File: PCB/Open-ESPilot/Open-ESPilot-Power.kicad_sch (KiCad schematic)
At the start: 29 parts, among them J15 VOUT, J2 VIN, J3 GND, M1 Clone "MP1584" module, Q3 AO3401A, U2 AMS1117-3.3, U3 INA219AxD, U8 AMS1117-3.3

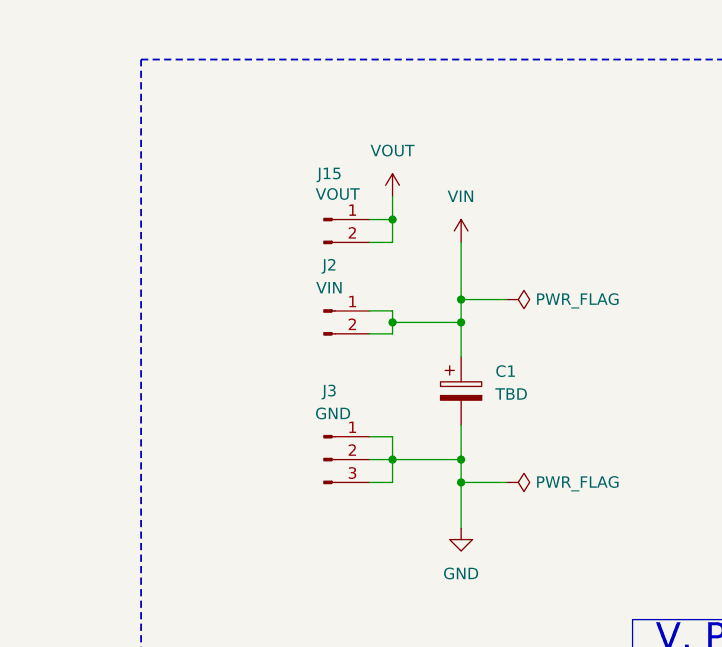
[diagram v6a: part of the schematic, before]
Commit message: Assigned footprints and components for the easy ones (R,C,JP,J)
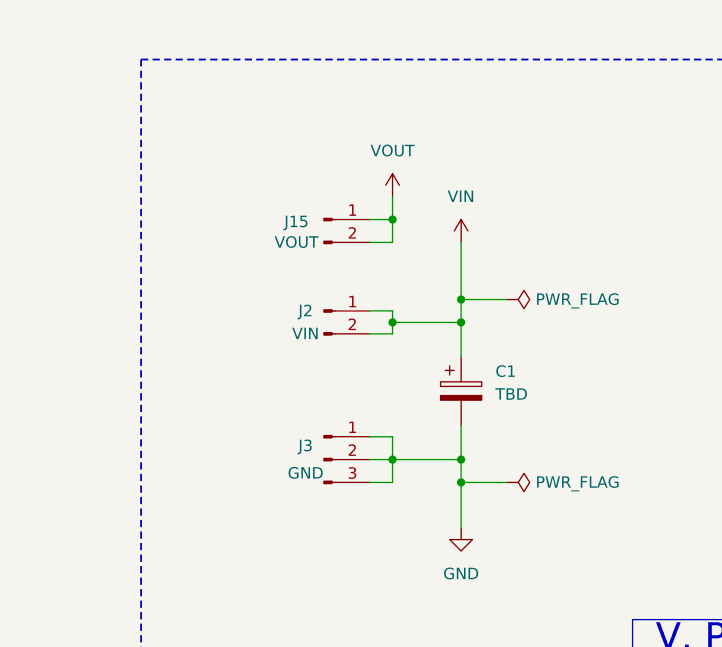
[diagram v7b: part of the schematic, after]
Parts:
- C10, C11, C12, C6, C7: footprint (none) -> Capacitor_SMD:C_0805_2012Metric_Pad1.18x1.45mm_HandSolder
- JP3, JP4: footprint (none) -> Jumper:SolderJumper-2_P1.3mm_Bridged2Bar_RoundedPad1.0x1.5mm
- JP5: footprint (none) -> Connector_PinHeader_2.54mm:PinHeader_1x03_P2.54mm_Vertical
- R12: footprint Resistor_THT:R_Axial_Shunt_L35.3mm_W9.5mm_PS25.40mm_P38.10mm -> (none)
- R13, R14, R8, R9: footprint (none) -> Resistor_SMD:R_0805_2012Metric_Pad1.20x1.40mm_HandSolder
- R15: footprint Resistor_SMD:R_0603_1608Metric_Pad0.98x0.95mm_HandSolder -> Resistor_SMD:R_0805_2012Metric_Pad1.20x1.40mm_HandSolder
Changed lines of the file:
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@@
 			)
 		)
-		(property "Footprint" ""
+		(property "Footprint" "Resistor_SMD:R_0805_2012Metric_Pad1.20x1.40mm_HandSolder"
 			(at 253.492 58.42 90)
 			(effects
@@
 			)
 		)
-		(property "Footprint" ""
+		(property "Footprint" "Jumper:SolderJumper-2_P1.3mm_Bridged2Bar_RoundedPad1.0x1.5mm"
 			(at 264.16 73.66 0)
 			(effects
@@
 		(dnp no)
 		(property "Reference" "J3"
-			(at 37.465 68.58 0)
+			(at 34.798 74.676 0)
 			(effects
 				(font
@@
 		)
 		(property "Value" "GND"
-			(at 37.846 71.12 0)
+			(at 34.798 77.724 0)
 			(effects
 				(font
@@
 			)
 		)
-		(property "Footprint" ""
+		(property "Footprint" "Capacitor_SMD:C_0805_2012Metric_Pad1.18x1.45mm_HandSolder"
 			(at 150.8252 133.35 0)
 			(effects
@@
 			)
 		)
-		(property "Footprint" ""
+		(property "Footprint" "Capacitor_SMD:C_0805_2012Metric_Pad1.18x1.45mm_HandSolder"
 			(at 118.4148 170.18 0)
 			(effects
@@
 			)
 		)
-		(property "Footprint" ""
+		(property "Footprint" "Jumper:SolderJumper-2_P1.3mm_Bridged2Bar_RoundedPad1.0x1.5mm"
 			(at 255.27 73.66 0)
 			(effects
@@
 			)
 		)
-		(property "Footprint" ""
+		(property "Footprint" "Connector_PinHeader_2.54mm:PinHeader_1x03_P2.54mm_Vertical"
 			(at 201.93 137.16 0)
 			(effects
@@
 			)
 		)
-		(property "Footprint" ""
+		(property "Footprint" "Capacitor_SMD:C_0805_2012Metric_Pad1.18x1.45mm_HandSolder"
 			(at 150.8252 170.18 0)
 			(effects
@@
 			)
 		)
-		(property "Footprint" "Resistor_THT:R_Axial_Shunt_L35.3mm_W9.5mm_PS25.40mm_P38.10mm"
+		(property "Footprint" ""
 			(at 207.01 53.848 90)
 			(effects
@@
 		(on_board yes)
 		(dnp no)
-		(fields_autoplaced yes)
 		(property "Reference" "J2"
-			(at 37.465 54.61 0)
+			(at 34.798 59.69 0)
 			(effects
 				(font
@@
 		)
 		(property "Value" "VIN"
-			(at 37.465 57.15 0)
+			(at 34.798 62.23 0)
 			(effects
 				(font
@@
 			)
 		)
-		(property "Footprint" ""
+		(property "Footprint" "Capacitor_SMD:C_0805_2012Metric_Pad1.18x1.45mm_HandSolder"
 			(at 118.4148 133.35 0)
 			(effects
@@
 			)
 		)
-		(property "Footprint" "Resistor_SMD:R_0603_1608Metric_Pad0.98x0.95mm_HandSolder"
+		(property "Footprint" "Resistor_SMD:R_0805_2012Metric_Pad1.20x1.40mm_HandSolder"
 			(at 243.84 140.97 0)
 			(effects
@@
 			)
 		)
-		(property "Footprint" ""
+		(property "Footprint" "Capacitor_SMD:C_0805_2012Metric_Pad1.18x1.45mm_HandSolder"
 			(at 53.0352 175.26 0)
 			(effects
@@
 		(dnp no)
 		(property "Reference" "J15"
-			(at 37.465 44.45 0)
+			(at 33.782 49.784 0)
 			(effects
 				(font
@@
 		)
 		(property "Value" "VOUT"
-			(at 38.354 46.736 0)
+			(at 33.782 52.07 0)
 			(effects
 				(font
@@
 			)
 		)
-		(property "Footprint" ""
+		(property "Footprint" "Resistor_SMD:R_0805_2012Metric_Pad1.20x1.40mm_HandSolder"
 			(at 262.382 58.42 90)
 			(effects
@@
 			)
 		)
-		(property "Footprint" ""
+		(property "Footprint" "Resistor_SMD:R_0805_2012Metric_Pad1.20x1.40mm_HandSolder"
 			(at 168.402 60.96 90)
 			(effects
@@
 			)
 		)
-		(property "Footprint" ""
+		(property "Footprint" "Resistor_SMD:R_0805_2012Metric_Pad1.20x1.40mm_HandSolder"
 			(at 168.402 73.66 90)
 			(effects

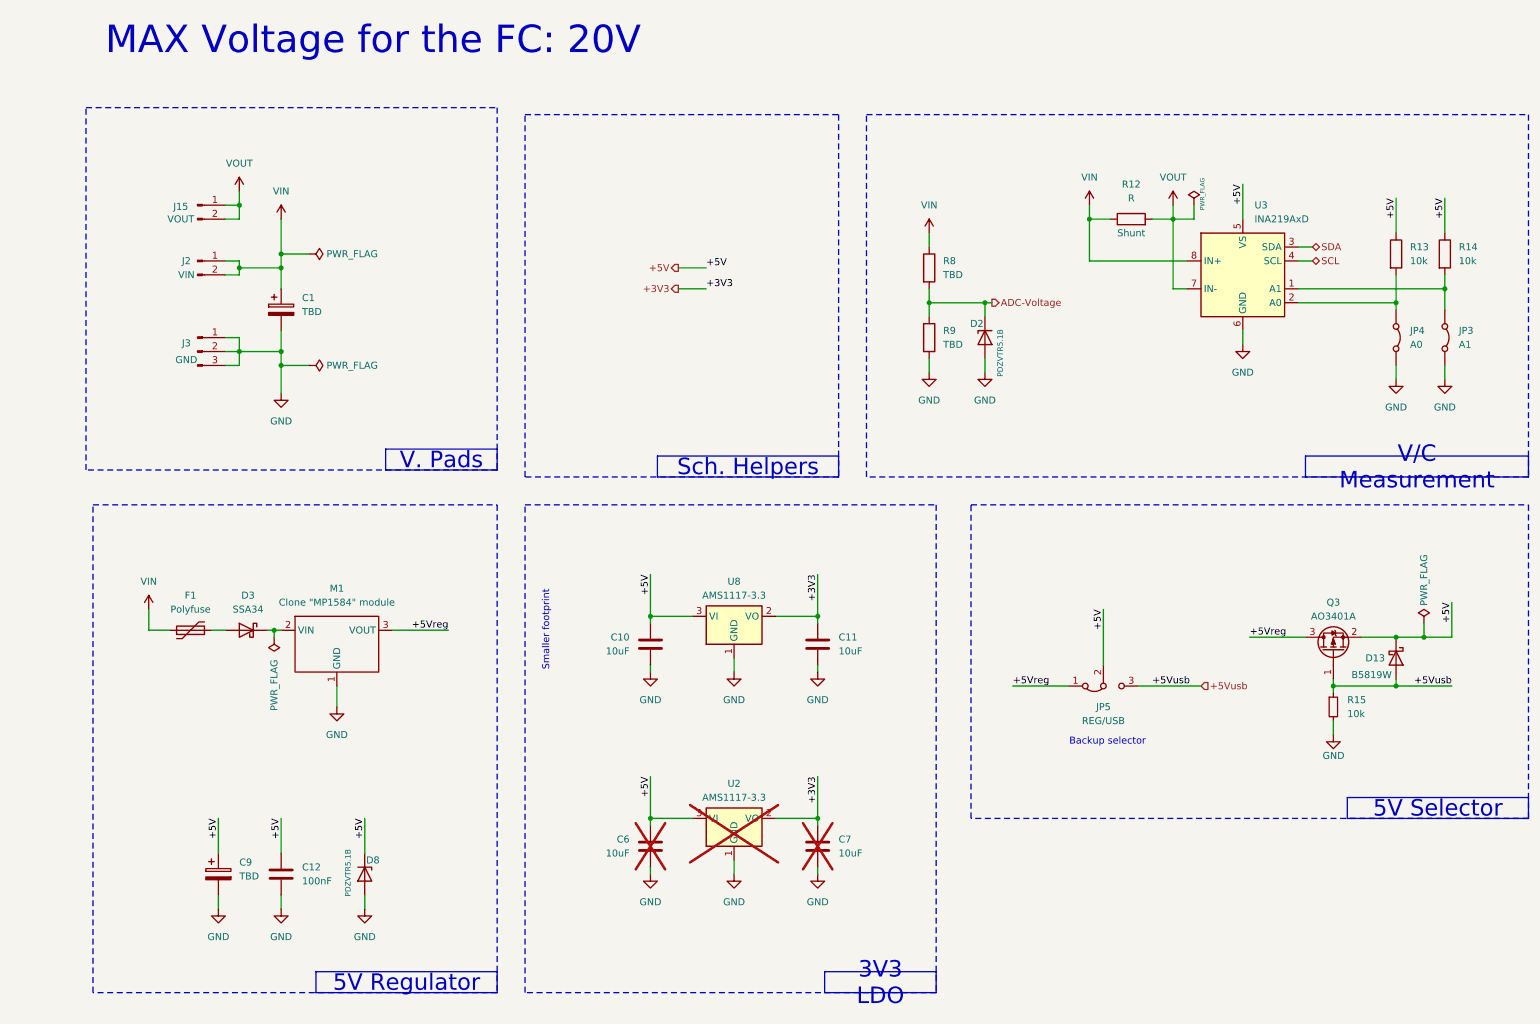
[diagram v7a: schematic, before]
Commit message: rearenged pins and moved polyfuse.
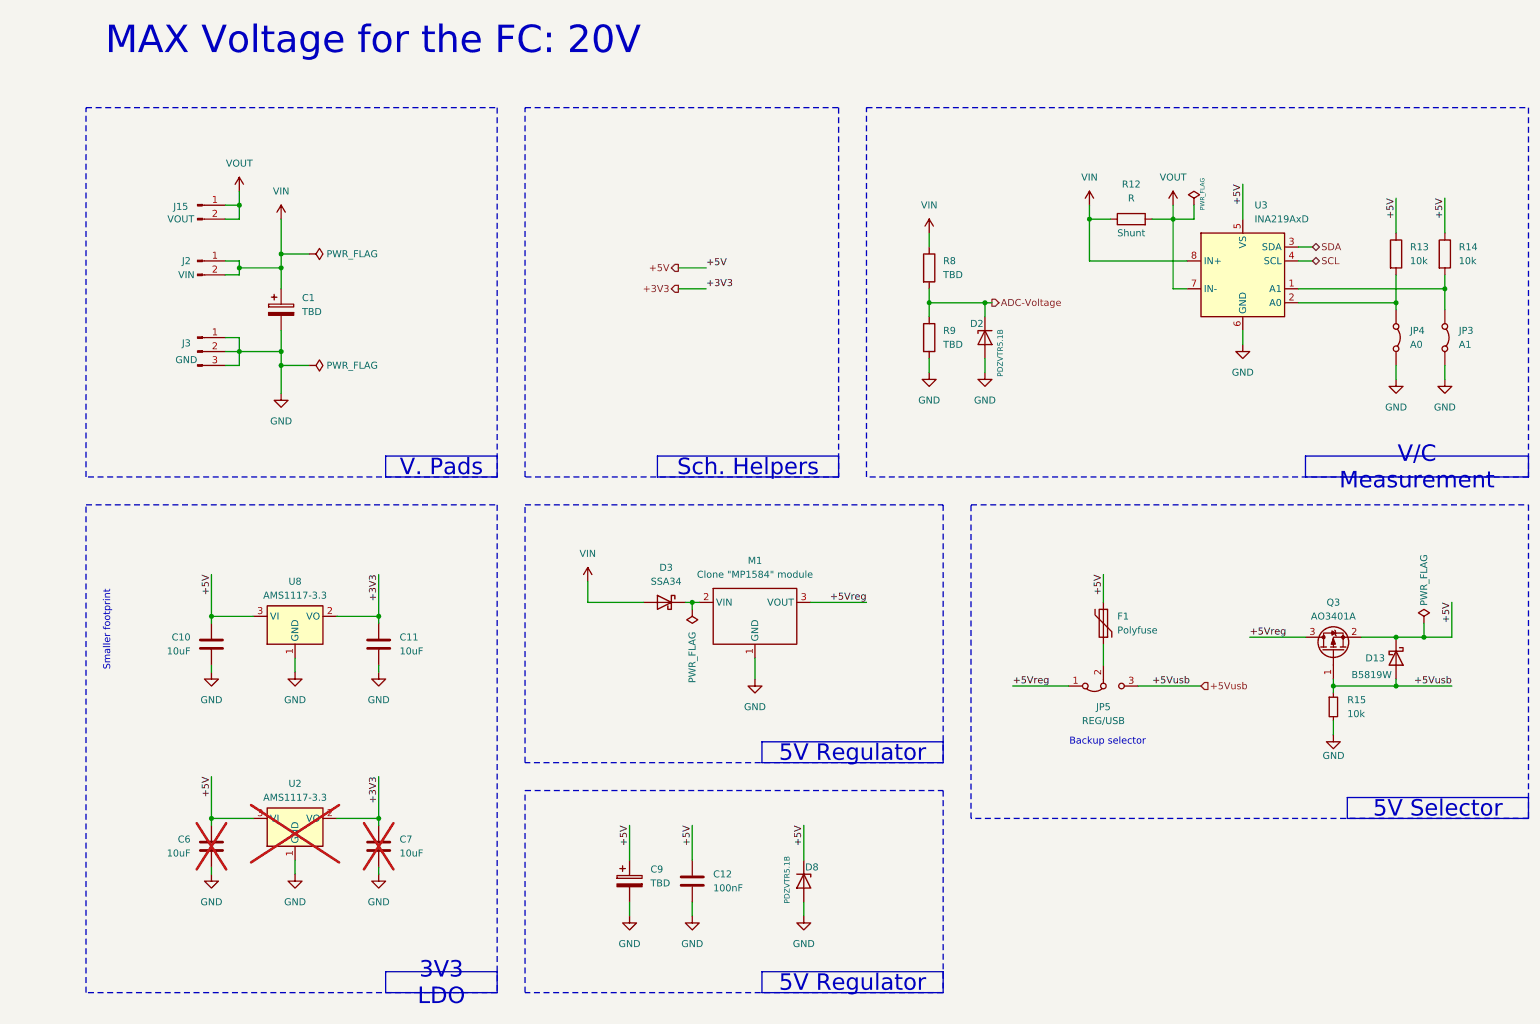
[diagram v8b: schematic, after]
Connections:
- net +5V: now also F1.2; no longer JP5.2 (C)
- net VIN: now also D3.2 (A); no longer F1.1
- new net: F1.1, JP5.2 (C)
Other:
- moved on the sheet: C10, C11, C12, C6, C7, C9, D3, D8, F1, M1, U2, U8
